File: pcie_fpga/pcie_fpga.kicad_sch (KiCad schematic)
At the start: 27 parts, among them J1 PMOD_Host_Conn_02x06, J2 PCIexpress_x8, J3 PMOD_Host_Conn_02x06, J4 PMOD_Host_Conn_02x06, J5 87832-1420, J6 Conn_02x03_Odd_Even, U2 XCAU10P-1FFVB676I, X1 ECS-2520MVQ-1000-BN-TR

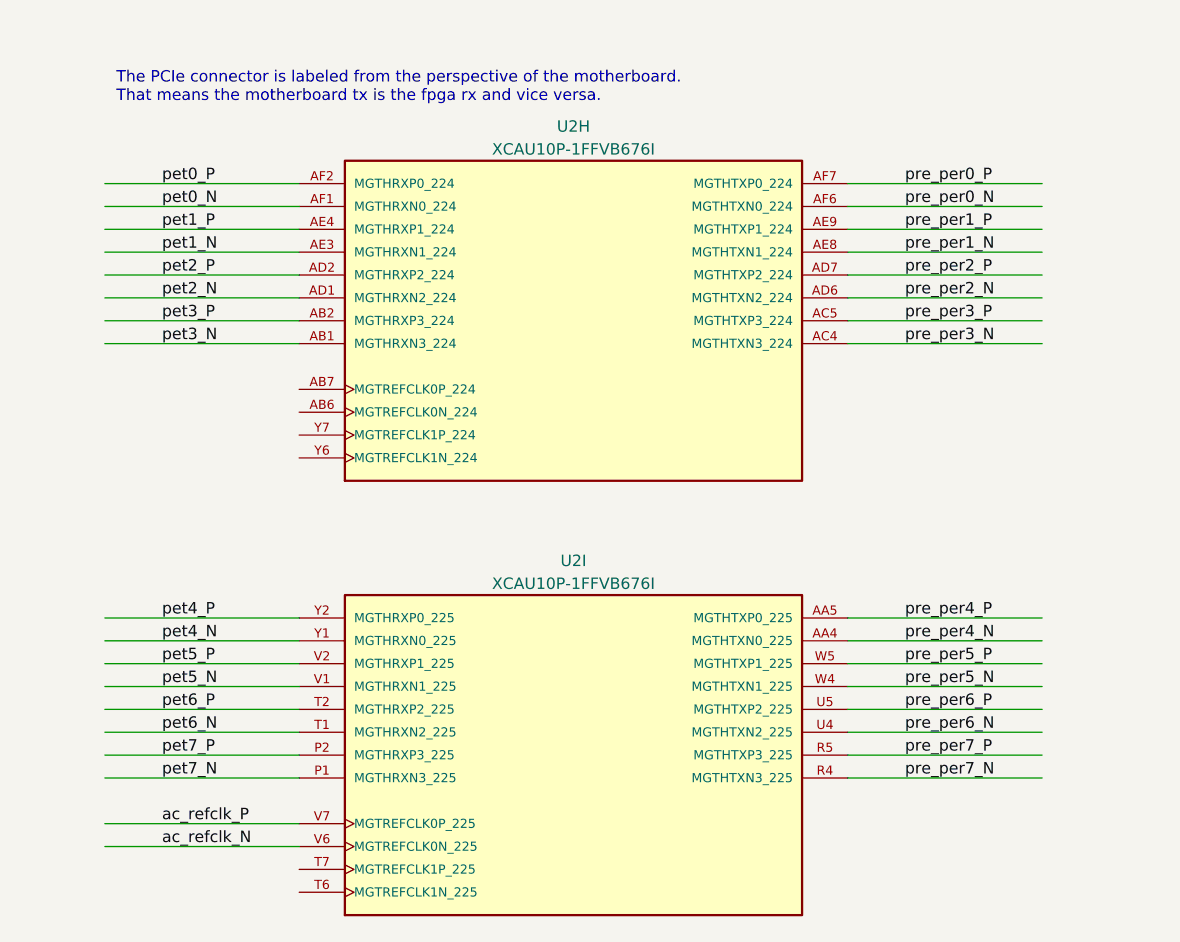
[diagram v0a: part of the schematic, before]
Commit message: swapped the pcie lanes for routing
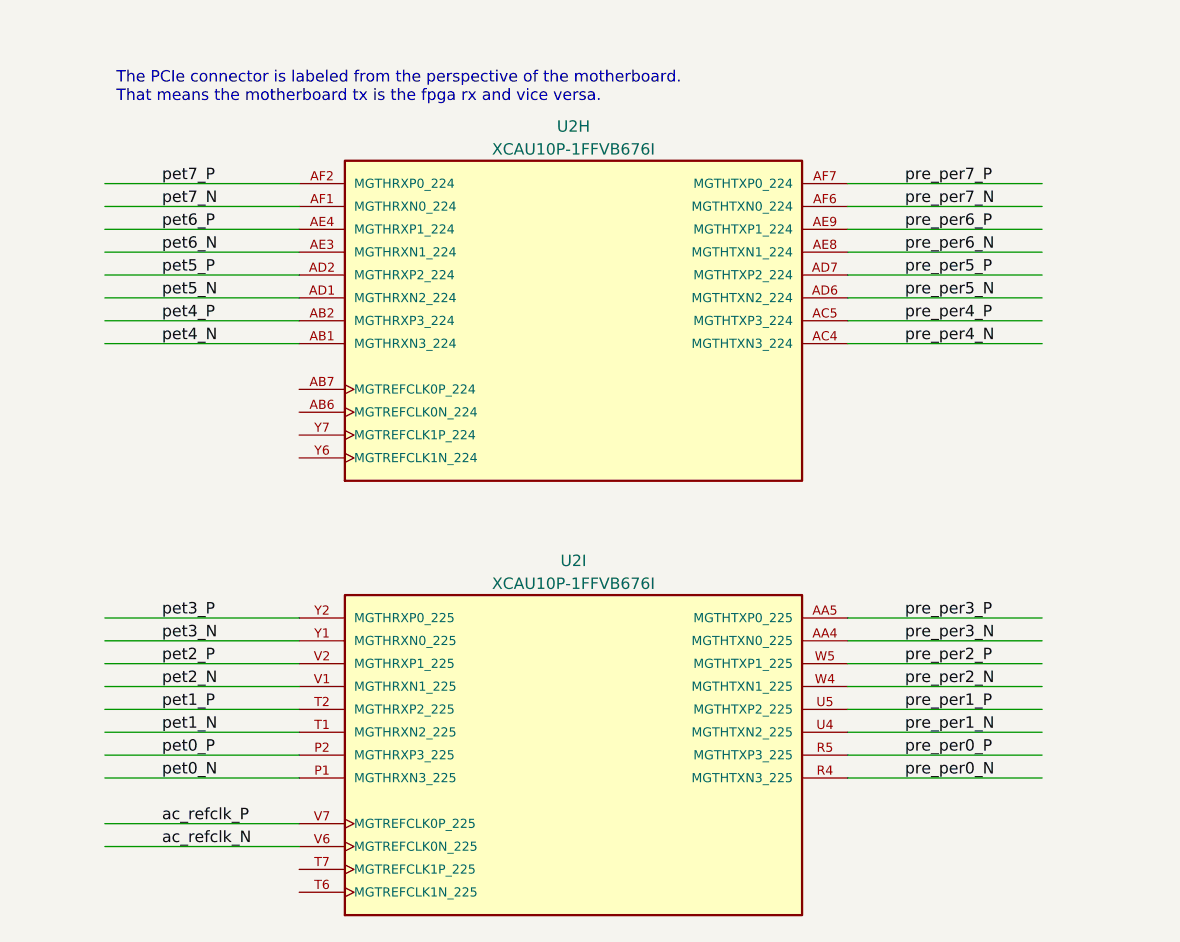
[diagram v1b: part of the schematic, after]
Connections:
- net pet0_N: now also U2.P1 (MGTHRXN3_225); no longer U2.AF1 (MGTHRXN0_224)
- net pet0_P: now also U2.P2 (MGTHRXP3_225); no longer U2.AF2 (MGTHRXP0_224)
- net pet1_N: now also U2.T1 (MGTHRXN2_225); no longer U2.AE3 (MGTHRXN1_224)
- net pet1_P: now also U2.T2 (MGTHRXP2_225); no longer U2.AE4 (MGTHRXP1_224)
- net pet2_N: now also U2.V1 (MGTHRXN1_225); no longer U2.AD1 (MGTHRXN2_224)
- net pet2_P: now also U2.V2 (MGTHRXP1_225); no longer U2.AD2 (MGTHRXP2_224)
- net pet3_N: now also U2.Y1 (MGTHRXN0_225); no longer U2.AB1 (MGTHRXN3_224)
- net pet3_P: now also U2.Y2 (MGTHRXP0_225); no longer U2.AB2 (MGTHRXP3_224)
- net pet4_N: now also U2.AB1 (MGTHRXN3_224); no longer U2.Y1 (MGTHRXN0_225)
- net pet4_P: now also U2.AB2 (MGTHRXP3_224); no longer U2.Y2 (MGTHRXP0_225)
- net pet5_N: now also U2.AD1 (MGTHRXN2_224); no longer U2.V1 (MGTHRXN1_225)
- net pet5_P: now also U2.AD2 (MGTHRXP2_224); no longer U2.V2 (MGTHRXP1_225)
- net pet6_N: now also U2.AE3 (MGTHRXN1_224); no longer U2.T1 (MGTHRXN2_225)
- net pet6_P: now also U2.AE4 (MGTHRXP1_224); no longer U2.T2 (MGTHRXP2_225)
- net pet7_N: now also U2.AF1 (MGTHRXN0_224); no longer U2.P1 (MGTHRXN3_225)
- net pet7_P: now also U2.AF2 (MGTHRXP0_224); no longer U2.P2 (MGTHRXP3_225)
- net pre_per0_N: now also U2.R4 (MGTHTXN3_225); no longer U2.AF6 (MGTHTXN0_224)
- net pre_per0_P: now also U2.R5 (MGTHTXP3_225); no longer U2.AF7 (MGTHTXP0_224)
- net pre_per1_N: now also U2.U4 (MGTHTXN2_225); no longer U2.AE8 (MGTHTXN1_224)
- net pre_per1_P: now also U2.U5 (MGTHTXP2_225); no longer U2.AE9 (MGTHTXP1_224)
- net pre_per2_N: now also U2.W4 (MGTHTXN1_225); no longer U2.AD6 (MGTHTXN2_224)
- net pre_per2_P: now also U2.W5 (MGTHTXP1_225); no longer U2.AD7 (MGTHTXP2_224)
- net pre_per3_N: now also U2.AA4 (MGTHTXN0_225); no longer U2.AC4 (MGTHTXN3_224)
- net pre_per3_P: now also U2.AA5 (MGTHTXP0_225); no longer U2.AC5 (MGTHTXP3_224)
- net pre_per4_N: now also U2.AC4 (MGTHTXN3_224); no longer U2.AA4 (MGTHTXN0_225)
- net pre_per4_P: now also U2.AC5 (MGTHTXP3_224); no longer U2.AA5 (MGTHTXP0_225)
- net pre_per5_N: now also U2.AD6 (MGTHTXN2_224); no longer U2.W4 (MGTHTXN1_225)
- net pre_per5_P: now also U2.AD7 (MGTHTXP2_224); no longer U2.W5 (MGTHTXP1_225)
- net pre_per6_N: now also U2.AE8 (MGTHTXN1_224); no longer U2.U4 (MGTHTXN2_225)
- net pre_per6_P: now also U2.AE9 (MGTHTXP1_224); no longer U2.U5 (MGTHTXP2_225)
- net pre_per7_N: now also U2.AF6 (MGTHTXN0_224); no longer U2.R4 (MGTHTXN3_225)
- net pre_per7_P: now also U2.AF7 (MGTHTXP0_224); no longer U2.R5 (MGTHTXP3_225)
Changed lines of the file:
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@@
     (effects (font (size 1.27 1.27)) (justify left bottom))
   )
-  (label "pre_per2_P" (at 293.37 292.1 0)
+  (label "pre_per5_P" (at 293.37 292.1 0)
     (effects (font (size 1.27 1.27)) (justify left bottom))
   )
@@
     (effects (font (size 1.27 1.27)) (justify left bottom))
   )
-  (label "pre_per0_N" (at 293.37 284.48 0)
+  (label "pre_per7_N" (at 293.37 284.48 0)
     (effects (font (size 1.27 1.27)) (justify left bottom))
   )
@@
     (effects (font (size 1.27 1.27)) (justify left bottom))
   )
-  (label "pet1_N" (at 210.82 289.56 0)
+  (label "pet6_N" (at 210.82 289.56 0)
     (effects (font (size 1.27 1.27)) (justify left bottom))
   )
@@
     (effects (font (size 1.27 1.27)) (justify left bottom))
   )
-  (label "pet4_P" (at 210.82 330.2 0)
+  (label "pet3_P" (at 210.82 330.2 0)
     (effects (font (size 1.27 1.27)) (justify left bottom))
   )
@@
     (effects (font (size 1.27 1.27)) (justify left bottom))
   )
-  (label "pre_per6_P" (at 293.37 340.36 0)
+  (label "pre_per1_P" (at 293.37 340.36 0)
     (effects (font (size 1.27 1.27)) (justify left bottom))
   )
@@
     (effects (font (size 1.27 1.27)) (justify left bottom))
   )
-  (label "pet6_N" (at 210.82 342.9 0)
+  (label "pet1_N" (at 210.82 342.9 0)
     (effects (font (size 1.27 1.27)) (justify left bottom))
   )
@@
     (effects (font (size 1.27 1.27)) (justify left bottom))
   )
-  (label "pre_per0_P" (at 293.37 281.94 0)
-    (effects (font (size 1.27 1.27)) (justify left bottom))
-  )
-  (label "pet0_N" (at 210.82 284.48 0)
+  (label "pre_per7_P" (at 293.37 281.94 0)
+    (effects (font (size 1.27 1.27)) (justify left bottom))
+  )
+  (label "pet7_N" (at 210.82 284.48 0)
     (effects (font (size 1.27 1.27)) (justify left bottom))
   )
@@
     (effects (font (size 1.27 1.27)) (justify left bottom))
   )
-  (label "pre_per5_N" (at 293.37 337.82 0)
-    (effects (font (size 1.27 1.27)) (justify left bottom))
-  )
-  (label "pre_per3_N" (at 293.37 299.72 0)
+  (label "pre_per2_N" (at 293.37 337.82 0)
+    (effects (font (size 1.27 1.27)) (justify left bottom))
+  )
+  (label "pre_per4_N" (at 293.37 299.72 0)
     (effects (font (size 1.27 1.27)) (justify left bottom))
   )
@@
     (effects (font (size 1.27 1.27)) (justify left bottom))
   )
-  (label "pre_per7_N" (at 293.37 347.98 0)
+  (label "pre_per0_N" (at 293.37 347.98 0)
     (effects (font (size 1.27 1.27)) (justify left bottom))
   )
@@
     (effects (font (size 1.27 1.27)) (justify left bottom))
   )
-  (label "pet5_N" (at 210.82 337.82 0)
-    (effects (font (size 1.27 1.27)) (justify left bottom))
-  )
-  (label "pet4_N" (at 210.82 332.74 0)
-    (effects (font (size 1.27 1.27)) (justify left bottom))
-  )
-  (label "pre_per1_P" (at 293.37 287.02 0)
+  (label "pet2_N" (at 210.82 337.82 0)
+    (effects (font (size 1.27 1.27)) (justify left bottom))
+  )
+  (label "pet3_N" (at 210.82 332.74 0)
+    (effects (font (size 1.27 1.27)) (justify left bottom))
+  )
+  (label "pre_per6_P" (at 293.37 287.02 0)
     (effects (font (size 1.27 1.27)) (justify left bottom))
   )
@@
     (effects (font (size 1.27 1.27)) (justify left bottom))
   )
-  (label "pet0_P" (at 210.82 281.94 0)
+  (label "pet7_P" (at 210.82 281.94 0)
     (effects (font (size 1.27 1.27)) (justify left bottom))
   )
@@
     (effects (font (size 1.27 1.27)) (justify left bottom))
   )
-  (label "pre_per2_N" (at 293.37 294.64 0)
+  (label "pre_per5_N" (at 293.37 294.64 0)
     (effects (font (size 1.27 1.27)) (justify left bottom))
   )
@@
     (effects (font (size 1.27 1.27)) (justify left bottom))
   )
-  (label "pet1_P" (at 210.82 287.02 0)
+  (label "pet6_P" (at 210.82 287.02 0)
     (effects (font (size 1.27 1.27)) (justify left bottom))
   )
@@
     (effects (font (size 1.27 1.27)) (justify left bottom))
   )
-  (label "pet6_P" (at 210.82 340.36 0)
+  (label "pet1_P" (at 210.82 340.36 0)
     (effects (font (size 1.27 1.27)) (justify left bottom))
   )
@@
     (effects (font (size 1.27 1.27)) (justify left bottom))
   )
-  (label "pre_per4_N" (at 293.37 332.74 0)
+  (label "pre_per3_N" (at 293.37 332.74 0)
     (effects (font (size 1.27 1.27)) (justify left bottom))
   )
@@
     (effects (font (size 1.27 1.27)) (justify left bottom))
   )
-  (label "pet3_P" (at 210.82 297.18 0)
-    (effects (font (size 1.27 1.27)) (justify left bottom))
-  )
-  (label "pet7_P" (at 210.82 345.44 0)
-    (effects (font (size 1.27 1.27)) (justify left bottom))
-  )
-  (label "pre_per7_P" (at 293.37 345.44 0)
-    (effects (font (size 1.27 1.27)) (justify left bottom))
-  )
-  (label "pet3_N" (at 210.82 299.72 0)
+  (label "pet4_P" (at 210.82 297.18 0)
+    (effects (font (size 1.27 1.27)) (justify left bottom))
+  )
+  (label "pet0_P" (at 210.82 345.44 0)
+    (effects (font (size 1.27 1.27)) (justify left bottom))
+  )
+  (label "pre_per0_P" (at 293.37 345.44 0)
+    (effects (font (size 1.27 1.27)) (justify left bottom))
+  )
+  (label "pet4_N" (at 210.82 299.72 0)
     (effects (font (size 1.27 1.27)) (justify left bottom))
   )
@@
     (effects (font (size 1.27 1.27)) (justify left bottom))
   )
-  (label "pre_per1_N" (at 293.37 289.56 0)
-    (effects (font (size 1.27 1.27)) (justify left bottom))
-  )
-  (label "pre_per5_P" (at 293.37 335.28 0)
+  (label "pre_per6_N" (at 293.37 289.56 0)
+    (effects (font (size 1.27 1.27)) (justify left bottom))
+  )
+  (label "pre_per2_P" (at 293.37 335.28 0)
     (effects (font (size 1.27 1.27)) (justify left bottom))
   )
@@
     (effects (font (size 1.27 1.27)) (justify left bottom))
   )
-  (label "pet2_N" (at 210.82 294.64 0)
+  (label "pet5_N" (at 210.82 294.64 0)
     (effects (font (size 1.27 1.27)) (justify left bottom))
   )
@@
     (effects (font (size 1.27 1.27)) (justify left bottom))
   )
-  (label "pet7_N" (at 210.82 347.98 0)
+  (label "pet0_N" (at 210.82 347.98 0)
     (effects (font (size 1.27 1.27)) (justify left bottom))
   )
@@
     (effects (font (size 1.27 1.27)) (justify left bottom))
   )
-  (label "pre_per4_P" (at 293.37 330.2 0)
-    (effects (font (size 1.27 1.27)) (justify left bottom))
-  )
-  (label "pre_per6_N" (at 293.37 342.9 0)
-    (effects (font (size 1.27 1.27)) (justify left bottom))
-  )
-  (label "pre_per3_P" (at 293.37 297.18 0)
+  (label "pre_per3_P" (at 293.37 330.2 0)
+    (effects (font (size 1.27 1.27)) (justify left bottom))
+  )
+  (label "pre_per1_N" (at 293.37 342.9 0)
+    (effects (font (size 1.27 1.27)) (justify left bottom))
+  )
+  (label "pre_per4_P" (at 293.37 297.18 0)
     (effects (font (size 1.27 1.27)) (justify left bottom))
   )
@@
     (effects (font (size 1.27 1.27)) (justify left bottom))
   )
-  (label "pet5_P" (at 210.82 335.28 0)
-    (effects (font (size 1.27 1.27)) (justify left bottom))
-  )
-  (label "pet2_P" (at 210.82 292.1 0)
-    (effects (font (size 1.27 1.27)) (justify left bottom))
-  )
+  (label "pet2_P" (at 210.82 335.28 0)
+    (effects (font (size 1.27 1.27)) (justify left bottom))
+  )
+  (label "pet5_P" (at 210.82 292.1 0)
+    (effects (font (size 1.27 1.27)) (justify left bottom))
+  )
